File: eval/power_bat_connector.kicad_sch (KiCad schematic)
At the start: 2 parts, among them U21 TS34031, U5 TS34031

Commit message: [layout] fan on bottom side, power area on top
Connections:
- net GNDPWR renamed GNDPWR_BAT

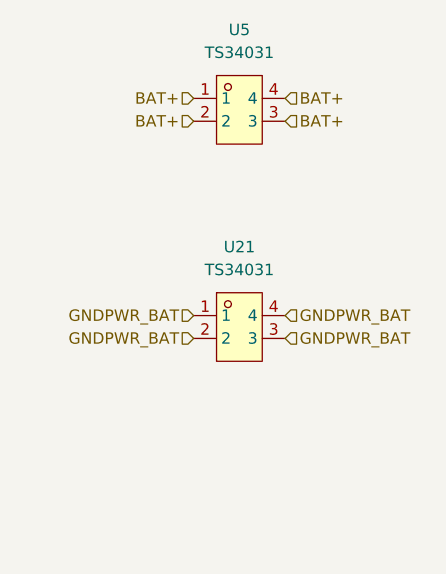
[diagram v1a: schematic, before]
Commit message: [trace] add high power trace
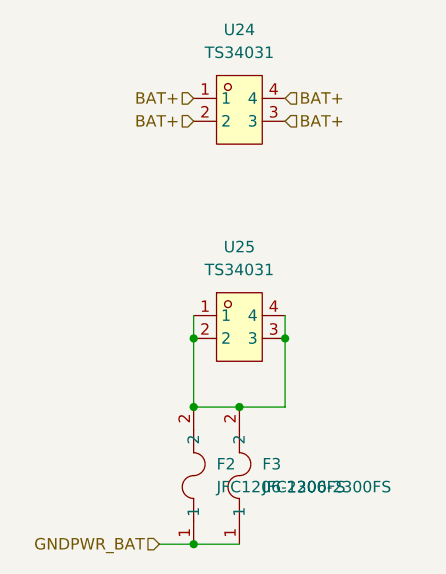
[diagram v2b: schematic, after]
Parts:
- added F2, F3: JFC1206-2300FS, EasyEDA:F1206, symbol EasyEDA:JFC1206-2300FS
- renumbered U5 to U24, U21 to U25
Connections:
- net GNDPWR_BAT: now also F2.1, F3.1; no longer U25.1, U25.2, U25.3, U25.4
- new net: F2.2, F3.2, U25.1, U25.2, U25.3, U25.4

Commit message: [layout&trace] layout 3 ntc sense.
Need more trace for 3 ntc, need add filter capacitor
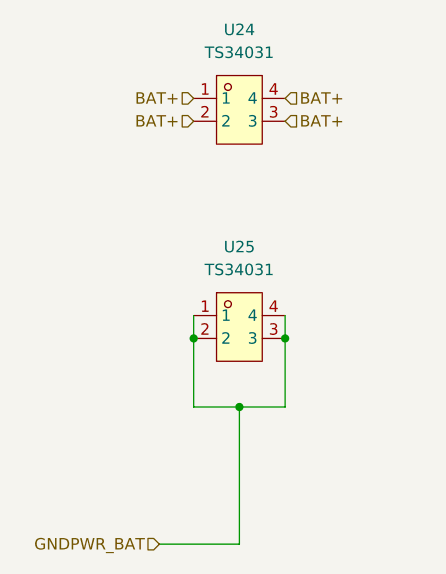
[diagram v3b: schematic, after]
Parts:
- removed F2, F3: JFC1206-2300FS, EasyEDA:F1206, symbol EasyEDA:JFC1206-2300FS
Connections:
- net GNDPWR_BAT: now also U25.1, U25.2, U25.3, U25.4
